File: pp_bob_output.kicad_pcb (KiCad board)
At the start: 2 copper layers, 98.8 x 72.1 mm, 38 parts, among them P4 13X2, U1 74LS540, U2 74LVC245, U3 74LS541

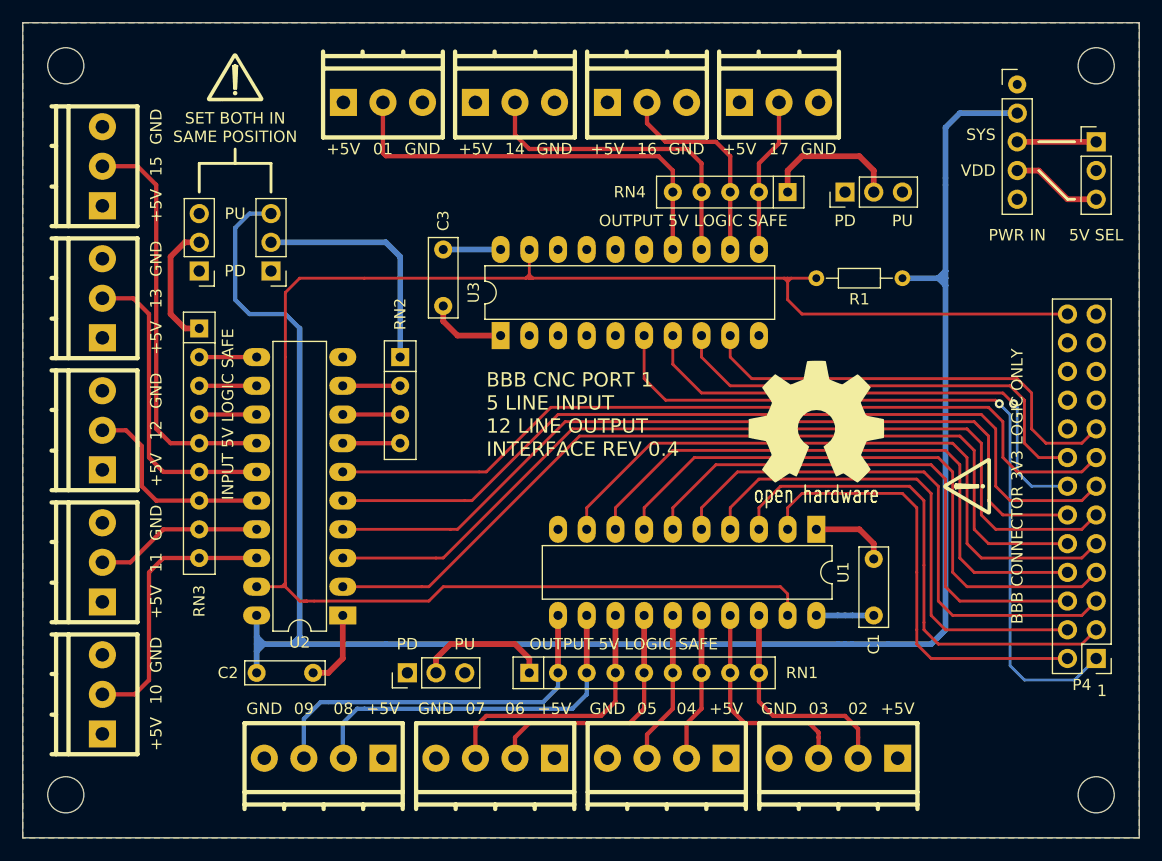
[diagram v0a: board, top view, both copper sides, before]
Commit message: Move 26 pin connector to allow for box type
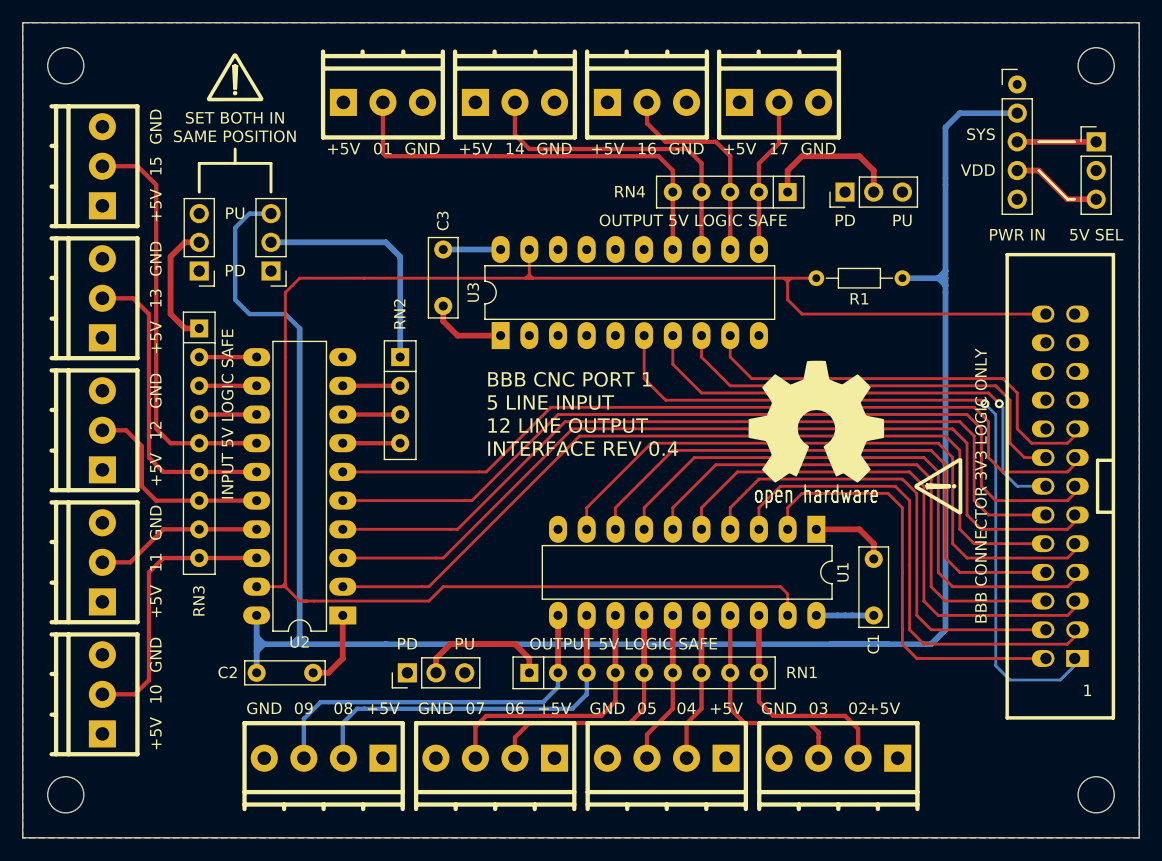
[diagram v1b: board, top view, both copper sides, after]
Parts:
- P4: footprint Pin_Headers:Pin_Header_Straight_2x13_Pitch2.54mm -> w_conn_strip:vasch_strip_13x2
- moved P4 15.6 mm to (117.2, 66.4), turned to 90 degrees
- moved G*** 2.54 mm to (106.4, 66.4)
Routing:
- net +3V3: track 171.8 -> 176.9 mm
- net CHIP_ENABLE: track 155.7 -> 153.8 mm
- net DB_11: track 79.3 -> 78.1 mm
- net DB_14: track 45.3 -> 44.0 mm
- net DB_02: track 40.3 -> 39.0 mm
- net DB_17: track 39.8 -> 38.6 mm
- net DB_16: track 40.2 -> 38.9 mm
- net DB_15: track 73.8 -> 72.5 mm
- net DB_13: track 76.5 -> 75.2 mm
- net DB_12: track 74.8 -> 73.6 mm
- net DB_10: track 77.7 -> 76.4 mm
- net DB_08: track 53.3 -> 52.1 mm
- net DB_07: track 54.2 -> 52.9 mm
- net DB_06: track 49.0 -> 47.7 mm
- net DB_05: track 49.9 -> 48.6 mm
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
